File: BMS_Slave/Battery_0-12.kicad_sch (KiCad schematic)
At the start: 16 parts, among them J10 Batt 7, J11 Batt 6, J12 Batt 2, J13 Batt 5, J14 Batt 1, J15 Batt 0, J2 Batt 13, J3 Batt 12, J4 Batt 11, J5 Batt 10, J6 Batt 9, J7 Batt 8, J8 Batt 4, J9 Batt 3

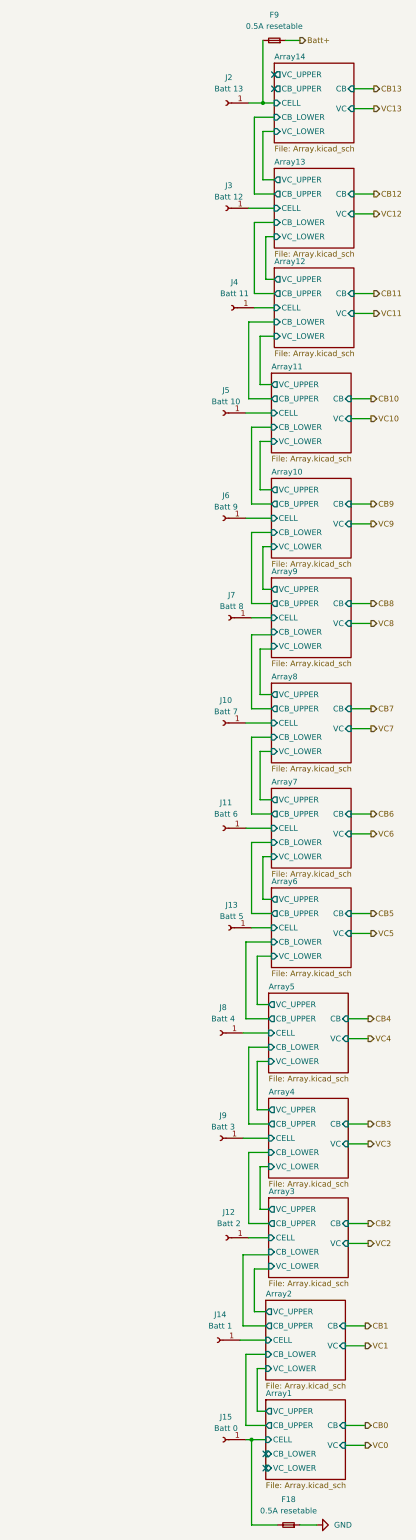
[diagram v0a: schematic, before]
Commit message: Dodano connectory hińskie zamiast padów, kontynuacja layoutu
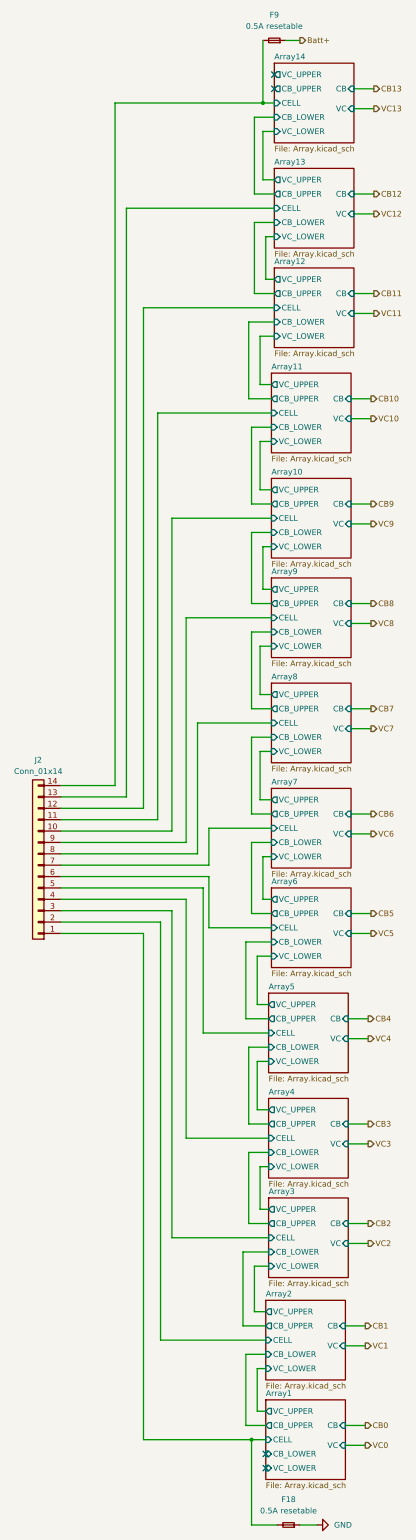
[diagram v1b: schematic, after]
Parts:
- removed J10: Batt 7, Connector_Wire:SolderWirePad_1x01_SMD_5x10mm, symbol Connector:Conn_01x01_Socket
- removed J11: Batt 6, Connector_Wire:SolderWirePad_1x01_SMD_5x10mm, symbol Connector:Conn_01x01_Socket
- removed J12: Batt 2, Connector_Wire:SolderWirePad_1x01_SMD_5x10mm, symbol Connector:Conn_01x01_Socket
- removed J13: Batt 5, Connector_Wire:SolderWirePad_1x01_SMD_5x10mm, symbol Connector:Conn_01x01_Socket
- removed J14: Batt 1, Connector_Wire:SolderWirePad_1x01_SMD_5x10mm, symbol Connector:Conn_01x01_Socket
- removed J15: Batt 0, Connector_Wire:SolderWirePad_1x01_SMD_5x10mm, symbol Connector:Conn_01x01_Socket
- removed J2: Batt 13, Connector_Wire:SolderWirePad_1x01_SMD_5x10mm, symbol Connector:Conn_01x01_Socket
- removed J3: Batt 12, Connector_Wire:SolderWirePad_1x01_SMD_5x10mm, symbol Connector:Conn_01x01_Socket
- removed J4: Batt 11, Connector_Wire:SolderWirePad_1x01_SMD_5x10mm, symbol Connector:Conn_01x01_Socket
- removed J5: Batt 10, Connector_Wire:SolderWirePad_1x01_SMD_5x10mm, symbol Connector:Conn_01x01_Socket
- removed J6: Batt 9, Connector_Wire:SolderWirePad_1x01_SMD_5x10mm, symbol Connector:Conn_01x01_Socket
- removed J7: Batt 8, Connector_Wire:SolderWirePad_1x01_SMD_5x10mm, symbol Connector:Conn_01x01_Socket
- removed J8: Batt 4, Connector_Wire:SolderWirePad_1x01_SMD_5x10mm, symbol Connector:Conn_01x01_Socket
- removed J9: Batt 3, Connector_Wire:SolderWirePad_1x01_SMD_5x10mm, symbol Connector:Conn_01x01_Socket
- added J2: Conn_01x14, Conn_custom:XY-XHB2.54-14A21, symbol Connector_Generic:Conn_01x14
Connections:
- net Array1/CELL: now also J2.1 (Pin_1)
- net Array10/CELL: now also J2.10 (Pin_10)
- net Array11/CELL: now also J2.11 (Pin_11)
- net Array12/CELL: now also J2.12 (Pin_12)
- net Array13/CELL: now also J2.13 (Pin_13)
- net Array14/CELL: now also J2.14 (Pin_14)
- net Array2/CELL: now also J2.2 (Pin_2)
- net Array3/CELL: now also J2.3 (Pin_3)
- net Array4/CELL: now also J2.4 (Pin_4)
- net Array5/CELL: now also J2.5 (Pin_5)
- net Array6/CELL: now also J2.6 (Pin_6)
- net Array7/CELL: now also J2.7 (Pin_7)
- net Array8/CELL: now also J2.8 (Pin_8)
- net Array9/CELL: now also J2.9 (Pin_9)
